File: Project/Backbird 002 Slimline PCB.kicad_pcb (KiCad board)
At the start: 2 copper layers, 14 x 116 mm, 8 parts

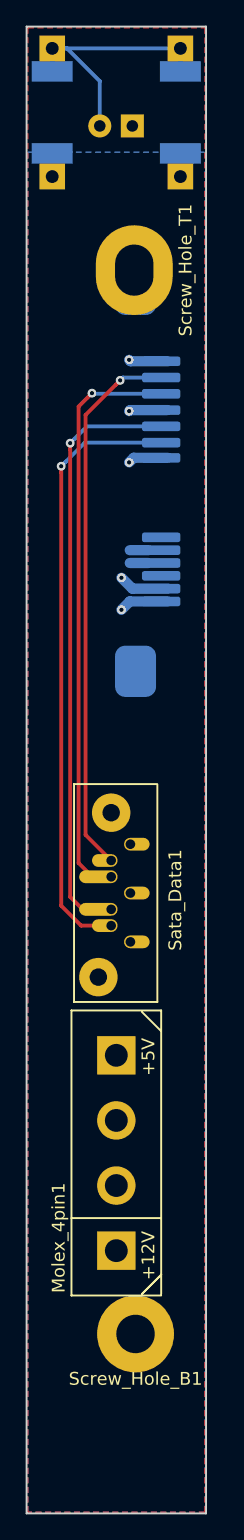
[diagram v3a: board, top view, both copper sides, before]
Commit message: Updated silkscreen to include description
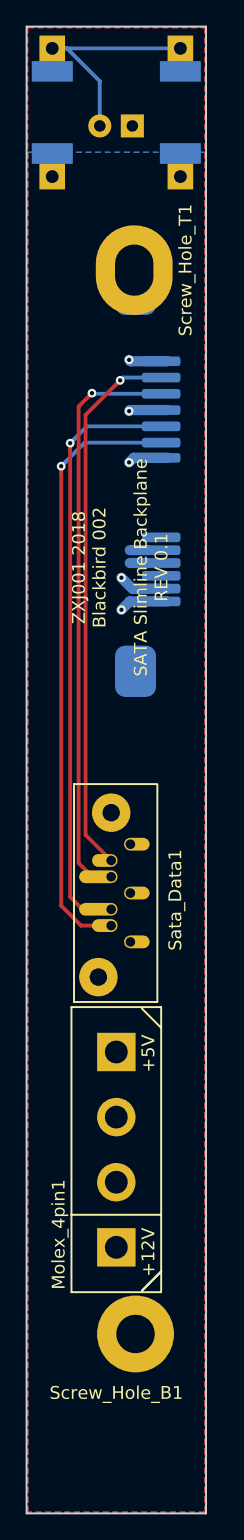
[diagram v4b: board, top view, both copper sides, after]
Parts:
- moved Molex_4pin1 0.26 mm to (107.3, 118.1)
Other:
- board text added: "ZXJ001 2018 Blackbird 002 SATA Slimline Backplane REV 0.1"
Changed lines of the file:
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@@
   (general
     (thickness 1.6)
-    (drawings 23)
+    (drawings 24)
     (tracks 60)
     (zones 0)
@@
   (page A4)
   (layers
-    (0 F.Cu signal hide)
+    (0 F.Cu signal)
     (31 B.Cu signal)
     (32 B.Adhes user)
     (33 F.Adhes user)
-    (34 B.Paste user)
-    (35 F.Paste user)
-    (36 B.SilkS user)
+    (34 B.Paste user hide)
+    (35 F.Paste user hide)
+    (36 B.SilkS user hide)
     (37 F.SilkS user)
     (38 B.Mask user)
@@
     (40 Dwgs.User user)
     (41 Cmts.User user)
-    (42 Eco1.User user)
-    (43 Eco2.User user)
+    (42 Eco1.User user hide)
+    (43 Eco2.User user hide)
     (44 Edge.Cuts user)
     (45 Margin user)
@@
   )
   (module ProjectFootprints:MOLEX_8981_0015244745 (layer F.Cu)
-    (at 107.3 118.36 90)
+    (at 107.3 118.1 90)
     (fp_text reference Molex_4pin1 (at -6.62 -4.5 90) (layer F.SilkS)
       (effects (font (size 1 1) (thickness 0.15)))
@@
   (module ProjectFootprints:Blackbird002_Slimline_PCB_Screw (layer F.Cu)
     (at 108.8 132.48)
-    (fp_text reference Screw_Hole_B1 (at 0 3.5) (layer F.SilkS)
+    (fp_text reference Screw_Hole_B1 (at -1.5 4.6) (layer F.SilkS)
       (effects (font (size 1 1) (thickness 0.15)))
     )
@@
     (pad 1 thru_hole oval (at 0 0 90) (size 7 6) (drill oval 4 3) (layers *.Cu *.Mask)
       (net 11 "Net-(Screw_Hole_T1-Pad1)"))
+  )
+  (gr_text "ZXJ001 2018\nBlackbird 002\n\nSATA Slimline Backplane\nREV 0.1" (at 107.6 72.68 90) (layer F.SilkS)
+    (effects (font (size 1 1) (thickness 0.2)))
   )
   (dimension 4 (width 0.3) (layer Eco1.User)
@@
   (segment (start 108.41 56.59) (end 108.3 56.48) (width 0.8) (layer B.Cu) (net 2))
   (segment (start 111.3 56.59) (end 108.41 56.59) (width 0.8) (layer B.Cu) (net 2))
+  (segment (start 112.3 40.3808) (end 112.3 42.18166) (width 0.3) (layer B.Cu) (net 2))
+  (segment (start 107.7 75.98) (end 108.35 75.33) (width 0.8) (layer B.Cu) (net 2))
+  (via (at 107.7 75.98) (size 0.6858) (drill 0.3302) (layers F.Cu B.Cu) (net 2))
+  (segment (start 108.35 75.33) (end 111.3 75.33) (width 0.8) (layer B.Cu) (net 2))
   (via (at 107.7 73.48) (size 0.6858) (drill 0.3302) (layers F.Cu B.Cu) (net 2))
+  (segment (start 108.55 74.33) (end 111.3 74.33) (width 0.8) (layer B.Cu) (net 2))
   (segment (start 107.7 73.48) (end 108.55 74.33) (width 0.8) (layer B.Cu) (net 2))
-  (segment (start 108.55 74.33) (end 111.3 74.33) (width 0.8) (layer B.Cu) (net 2))
-  (via (at 107.7 75.98) (size 0.6858) (drill 0.3302) (layers F.Cu B.Cu) (net 2))
-  (segment (start 107.7 75.98) (end 108.35 75.33) (width 0.8) (layer B.Cu) (net 2))
-  (segment (start 108.35 75.33) (end 111.3 75.33) (width 0.8) (layer B.Cu) (net 2))
-  (segment (start 112.3 40.3808) (end 112.3 42.18166) (width 0.3) (layer B.Cu) (net 2))
   (segment (start 109.8 71.33) (end 108.35 71.33) (width 0.8) (layer B.Cu) (net 3))
   (segment (start 109.8 72.33) (end 108.35 72.33) (width 0.8) (layer B.Cu) (net 3))
+  (segment (start 106.9 100.62) (end 104.555067 100.62) (width 0.3) (layer F.Cu) (net 4))
+  (segment (start 103 65.264933) (end 103 64.78) (width 0.3) (layer F.Cu) (net 4))
+  (segment (start 103 99.064933) (end 103 65.264933) (width 0.3) (layer F.Cu) (net 4))
   (segment (start 104.555067 100.62) (end 103 99.064933) (width 0.3) (layer F.Cu) (net 4))
-  (segment (start 106.9 100.62) (end 104.555067 100.62) (width 0.3) (layer F.Cu) (net 4))
+  (via (at 103 64.78) (size 0.6858) (drill 0.3302) (layers F.Cu B.Cu) (net 4))
   (segment (start 103.342899 64.437101) (end 103 64.78) (width 0.3) (layer B.Cu) (net 4))
+  (segment (start 111.3 62.94) (end 104.84 62.94) (width 0.3) (layer B.Cu) (net 4))
   (segment (start 104.84 62.94) (end 103.342899 64.437101) (width 0.3) (layer B.Cu) (net 4))
-  (segment (start 103 99.064933) (end 103 65.264933) (width 0.3) (layer F.Cu) (net 4))
-  (segment (start 111.3 62.94) (end 104.84 62.94) (width 0.3) (layer B.Cu) (net 4))
-  (segment (start 103 65.264933) (end 103 64.78) (width 0.3) (layer F.Cu) (net 4))
-  (via (at 103 64.78) (size 0.6858) (drill 0.3302) (layers F.Cu B.Cu) (net 4))
   (segment (start 106.9 99.35) (end 106.238934 99.35) (width 0.1524) (layer F.Cu) (net 5))
+  (segment (start 111.3 61.67) (end 105.010002 61.67) (width 0.3) (layer B.Cu) (net 5))
+  (segment (start 105.010002 61.67) (end 104.042901 62.637101) (width 0.3) (layer B.Cu) (net 5))
   (via (at 103.700002 62.98) (size 0.6858) (drill 0.3302) (layers F.Cu B.Cu) (net 5))
-  (segment (start 105.010002 61.67) (end 104.042901 62.637101) (width 0.3) (layer B.Cu) (net 5))
-  (segment (start 111.3 61.67) (end 105.010002 61.67) (width 0.3) (layer B.Cu) (net 5))
+  (segment (start 104.67 99.35) (end 103.700002 98.380002) (width 0.3) (layer F.Cu) (net 5))
+  (segment (start 103.700002 63.464933) (end 103.700002 62.98) (width 0.3) (layer F.Cu) (net 5))
+  (segment (start 106.9 99.35) (end 104.67 99.35) (width 0.3) (layer F.Cu) (net 5))
   (segment (start 104.042901 62.637101) (end 103.700002 62.98) (width 0.3) (layer B.Cu) (net 5))
-  (segment (start 104.67 99.35) (end 103.700002 98.380002) (width 0.3) (layer F.Cu) (net 5))
-  (segment (start 106.9 99.35) (end 104.67 99.35) (width 0.3) (layer F.Cu) (net 5))
   (segment (start 103.700002 98.380002) (end 103.700002 63.464933) (width 0.3) (layer F.Cu) (net 5))
-  (segment (start 103.700002 63.464933) (end 103.700002 62.98) (width 0.3) (layer F.Cu) (net 5))
+  (segment (start 105.45 59.13) (end 105.4 59.08) (width 0.3) (layer B.Cu) (net 6))
+  (segment (start 104.357101 60.122899) (end 105.057101 59.422899) (width 0.3) (layer F.Cu) (net 6))
+  (segment (start 111.3 59.13) (end 105.45 59.13) (width 0.3) (layer B.Cu) (net 6))
+  (segment (start 106.9 96.81) (end 105.43 96.81) (width 0.3) (layer F.Cu) (net 6))
+  (segment (start 105.057101 59.422899) (end 105.4 59.08) (width 0.3) (layer F.Cu) (net 6))
+  (segment (start 104.357101 95.737101) (end 104.357101 60.122899) (width 0.3) (layer F.Cu) (net 6))
+  (segment (start 105.43 96.81) (end 104.357101 95.737101) (width 0.3) (layer F.Cu) (net 6))
   (via (at 105.4 59.08) (size 0.6858) (drill 0.3302) (layers F.Cu B.Cu) (net 6))
-  (segment (start 105.43 96.81) (end 104.357101 95.737101) (width 0.3) (layer F.Cu) (net 6))
-  (segment (start 111.3 59.13) (end 105.45 59.13) (width 0.3) (layer B.Cu) (net 6))
-  (segment (start 104.357101 95.737101) (end 104.357101 60.122899) (width 0.3) (layer F.Cu) (net 6))
-  (segment (start 104.357101 60.122899) (end 105.057101 59.422899) (width 0.3) (layer F.Cu) (net 6))
-  (segment (start 105.057101 59.422899) (end 105.4 59.08) (width 0.3) (layer F.Cu) (net 6))
-  (segment (start 105.45 59.13) (end 105.4 59.08) (width 0.3) (layer B.Cu) (net 6))
-  (segment (start 106.9 96.81) (end 105.43 96.81) (width 0.3) (layer F.Cu) (net 6))
-  (via (at 107.599992 58.08) (size 0.6858) (drill 0.3302) (layers F.Cu B.Cu) (net 7))
   (segment (start 107.819992 57.86) (end 107.599992 58.08) (width 0.3) (layer B.Cu) (net 7))
   (segment (start 111.3 57.86) (end 107.819992 57.86) (width 0.3) (layer B.Cu) (net 7))
   (segment (start 106.9 95.54) (end 104.9 93.54) (width 0.3) (layer F.Cu) (net 7))
-  (segment (start 107.257093 58.422899) (end 107.599992 58.08) (width 0.3) (layer F.Cu) (net 7))
+  (via (at 107.599992 58.08) (size 0.6858) (drill 0.3302) (layers F.Cu B.Cu) (net 7))
   (segment (start 104.9 93.54) (end 104.9 60.779992) (width 0.3) (layer F.Cu) (net 7))
   (segment (start 104.9 60.779992) (end 107.257093 58.422899) (width 0.3) (layer F.Cu) (net 7))
+  (segment (start 107.257093 58.422899) (end 107.599992 58.08) (width 0.3) (layer F.Cu) (net 7))
   (zone (net 3) (net_name +5V) (layer B.Cu) (hatch edge 0.508)
     (connect_pads (clearance 0.508))

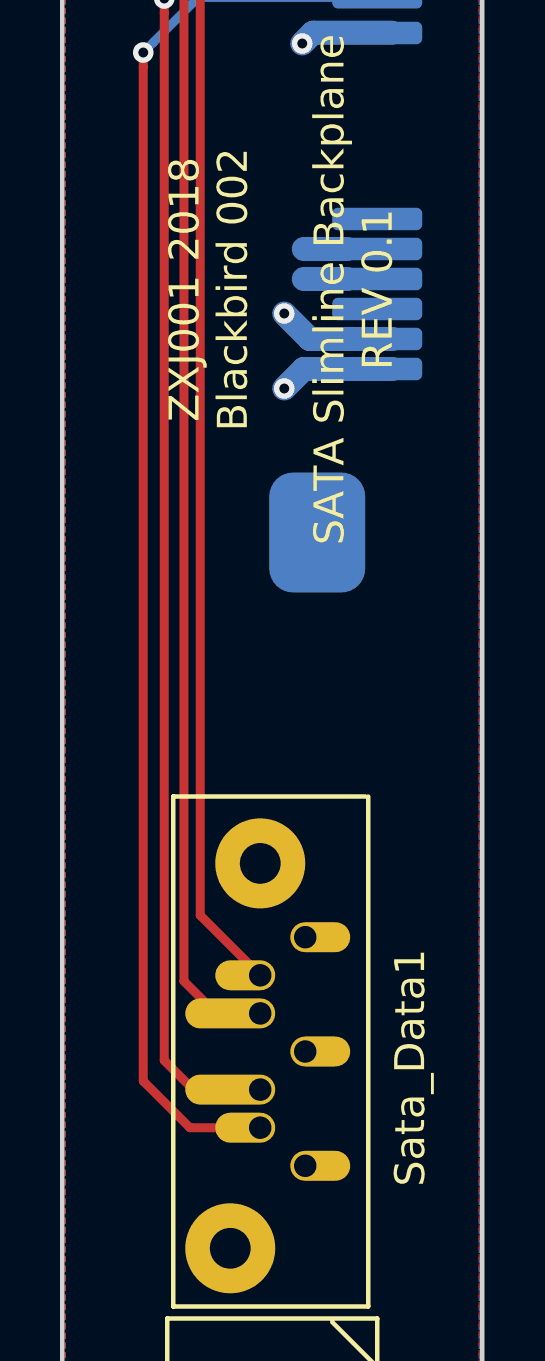
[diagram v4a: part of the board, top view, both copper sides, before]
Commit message: Fix SATA padding by having the drill in the center of the pad to meet OSHPark's expectations.
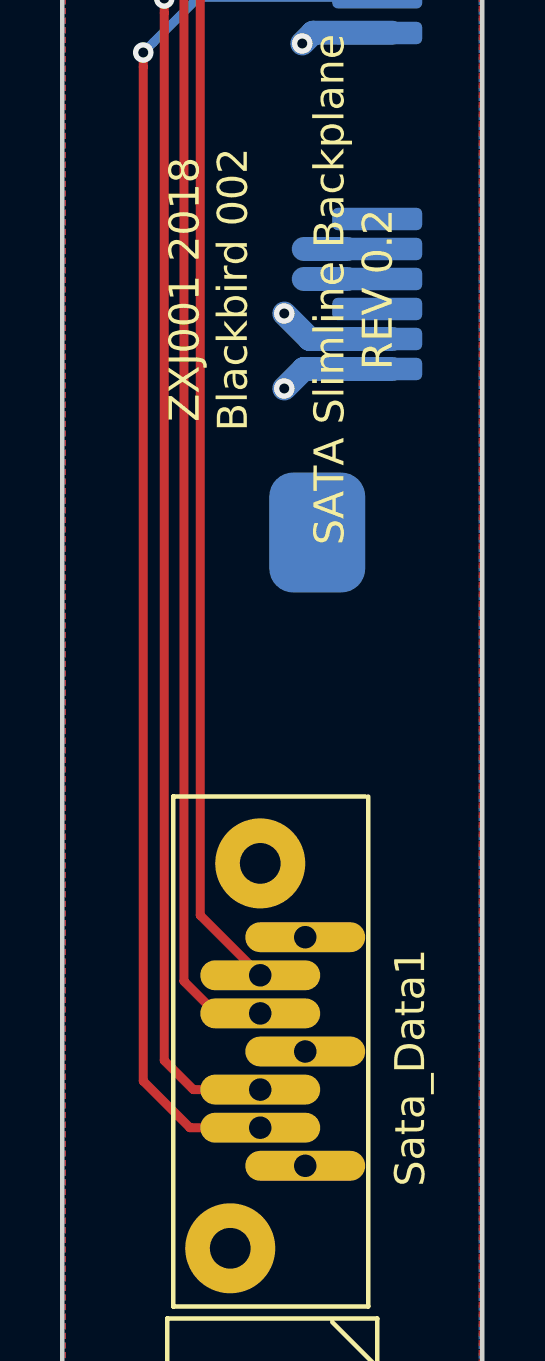
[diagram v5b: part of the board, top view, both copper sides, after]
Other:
- board text added: "ZXJ001 2018 Blackbird 002 SATA Slimline Backplane REV 0.2"
- board text removed: "ZXJ001 2018 Blackbird 002 SATA Slimline Backplane REV 0.1"
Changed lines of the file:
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@@
     (visible_elements FFFFFF7F)
     (pcbplotparams
-      (layerselection 0x010fc_ffffffff)
-      (usegerberextensions false)
+      (layerselection 0x010f0_ffffffff)
+      (usegerberextensions true)
       (usegerberattributes false)
       (usegerberadvancedattributes false)
@@
       (outputformat 1)
       (mirror false)
-      (drillshape 1)
+      (drillshape 0)
       (scaleselection 1)
-      (outputdirectory ""))
+      (outputdirectory Plots/))
   )
   (net 0 "")
@@
     (add_net "Net-(Screw_Hole_T1-Pad1)")
   )
+  (module ProjectFootprints:SATA_DATA_678007005_CustomPad (layer F.Cu)
+    (at 111.3 106.48 90)
+    (fp_text reference Sata_Data1 (at 7.86 0.6 90) (layer F.SilkS)
+      (effects (font (size 1 1) (thickness 0.15)))
+    )
+    (fp_text value Conn_01x07 (at 8.4 -9.504 90) (layer F.Fab)
+      (effects (font (size 1 1) (thickness 0.15)))
+    )
+    (fp_line (start 16.9 -7.3) (end 16.9 -0.9) (layer F.SilkS) (width 0.15))
+    (fp_line (start -0.1 -7.3) (end 16.9 -7.3) (layer F.SilkS) (width 0.15))
+    (fp_line (start -0.1 -0.8) (end -0.1 -7.3) (layer F.SilkS) (width 0.15))
+    (fp_line (start -0.1 -0.8) (end 16.9 -0.8) (layer F.SilkS) (width 0.15))
+    (pad 1 thru_hole oval (at 12.21 -2.9 270) (size 1 4) (drill 0.75) (layers *.Cu *.Mask)
+      (net 2 GND))
+    (pad 4 thru_hole oval (at 8.4 -2.9 270) (size 1 4) (drill 0.75) (layers *.Cu *.Mask)
+      (net 2 GND))
+    (pad 7 thru_hole oval (at 4.59 -2.9 270) (size 1 4) (drill 0.75) (layers *.Cu *.Mask)
+      (net 2 GND))
+    (pad 2 thru_hole oval (at 10.94 -4.4 90) (size 1 4) (drill 0.75) (layers *.Cu *.Mask)
+      (net 7 A+))
+    (pad 3 thru_hole oval (at 9.67 -4.4 90) (size 1 4) (drill 0.75) (layers *.Cu *.Mask)
+      (net 6 A-))
+    (pad 5 thru_hole oval (at 7.13 -4.4 90) (size 1 4) (drill 0.75) (layers *.Cu *.Mask)
+      (net 5 B-))
+    (pad 8 thru_hole circle (at 1.84 -5.4 90) (size 3 3) (drill 1.36) (layers *.Cu *.Mask))
+    (pad 8 thru_hole circle (at 14.67 -4.4 90) (size 3 3) (drill 1.36) (layers *.Cu *.Mask))
+    (pad 6 thru_hole oval (at 5.86 -4.4 90) (size 1 4) (drill 0.75) (layers *.Cu *.Mask)
+      (net 4 B+))
+  )
   (module ProjectFootprints:SATA_SLIMLINE_RECPT_1735539-2 (layer B.Cu)
     (at 108.8 65.88 90)
@@
     (pad 2 thru_hole rect (at 5.00126 0 90) (size 1.99898 1.99898) (drill 1.00076) (layers *.Cu *.Mask)
       (net 3 +5V))
-  )
-  (module ProjectFootprints:SATA_DATA_678007005_CustomPad (layer F.Cu)
-    (at 111.3 106.48 90)
-    (fp_text reference Sata_Data1 (at 7.86 0.6 90) (layer F.SilkS)
-      (effects (font (size 1 1) (thickness 0.15)))
-    )
-    (fp_text value Conn_01x07 (at 8.4 -9.504 90) (layer F.Fab)
-      (effects (font (size 1 1) (thickness 0.15)))
-    )
-    (fp_line (start 16.9 -7.3) (end 16.9 -0.9) (layer F.SilkS) (width 0.15))
-    (fp_line (start -0.1 -7.3) (end 16.9 -7.3) (layer F.SilkS) (width 0.15))
-    (fp_line (start -0.1 -0.8) (end -0.1 -7.3) (layer F.SilkS) (width 0.15))
-    (fp_line (start -0.1 -0.8) (end 16.9 -0.8) (layer F.SilkS) (width 0.15))
-    (pad 1 thru_hole oval (at 12.21 -2.9 270) (size 1 2) (drill 0.75 (offset 0 -0.5)) (layers *.Cu *.Mask)
-      (net 2 GND))
-    (pad 4 thru_hole oval (at 8.4 -2.9 270) (size 1 2) (drill 0.75 (offset 0 -0.5)) (layers *.Cu *.Mask)
-      (net 2 GND))
-    (pad 7 thru_hole oval (at 4.59 -2.9 270) (size 1 2) (drill 0.75 (offset 0 -0.5)) (layers *.Cu *.Mask)
-      (net 2 GND))
-    (pad 2 thru_hole oval (at 10.94 -4.4 90) (size 1 2) (drill 0.75 (offset 0 -0.5)) (layers *.Cu *.Mask)
-      (net 7 A+))
-    (pad 3 thru_hole oval (at 9.67 -4.4 90) (size 1 3) (drill 0.75 (offset 0 -1)) (layers *.Cu *.Mask)
-      (net 6 A-))
-    (pad 5 thru_hole oval (at 7.13 -4.4 90) (size 1 3) (drill 0.75 (offset 0 -1)) (layers *.Cu *.Mask)
-      (net 5 B-))
-    (pad 8 thru_hole circle (at 1.84 -5.4 90) (size 3 3) (drill 1.36) (layers *.Cu *.Mask))
-    (pad 8 thru_hole circle (at 14.67 -4.4 90) (size 3 3) (drill 1.36) (layers *.Cu *.Mask))
-    (pad 6 thru_hole oval (at 5.86 -4.4 90) (size 1 2) (drill 0.75 (offset 0 -0.5)) (layers *.Cu *.Mask)
-      (net 4 B+))
   )
   (module LEDs:LED_D1.8mm_W3.3mm_H2.4mm (layer B.Cu)
@@
       (net 11 "Net-(Screw_Hole_T1-Pad1)"))
   )
-  (gr_text "ZXJ001 2018\nBlackbird 002\n\nSATA Slimline Backplane\nREV 0.1" (at 107.6 72.68 90) (layer F.SilkS)
+  (gr_text "ZXJ001 2018\nBlackbird 002\n\nSATA Slimline Backplane\nREV 0.2" (at 107.6 72.68 90) (layer F.SilkS)
     (effects (font (size 1 1) (thickness 0.2)))
   )
@@
   (segment (start 109.8 71.33) (end 108.35 71.33) (width 0.8) (layer B.Cu) (net 3))
   (segment (start 109.8 72.33) (end 108.35 72.33) (width 0.8) (layer B.Cu) (net 3))
-  (segment (start 106.9 100.62) (end 104.555067 100.62) (width 0.3) (layer F.Cu) (net 4))
-  (segment (start 103 65.264933) (end 103 64.78) (width 0.3) (layer F.Cu) (net 4))
-  (segment (start 103 99.064933) (end 103 65.264933) (width 0.3) (layer F.Cu) (net 4))
-  (segment (start 104.555067 100.62) (end 103 99.064933) (width 0.3) (layer F.Cu) (net 4))
-  (via (at 103 64.78) (size 0.6858) (drill 0.3302) (layers F.Cu B.Cu) (net 4))
-  (segment (start 103.342899 64.437101) (end 103 64.78) (width 0.3) (layer B.Cu) (net 4))
-  (segment (start 111.3 62.94) (end 104.84 62.94) (width 0.3) (layer B.Cu) (net 4))
-  (segment (start 104.84 62.94) (end 103.342899 64.437101) (width 0.3) (layer B.Cu) (net 4))
+  (segment (start 104.84 62.94) (end 103.342899 64.437101) (width 0.3) (layer B.Cu) (net 4) (status 1000000))
+  (segment (start 103 65.264933) (end 103 64.78) (width 0.3) (layer F.Cu) (net 4) (status 1000000))
+  (segment (start 111.3 62.94) (end 104.84 62.94) (width 0.3) (layer B.Cu) (net 4) (status 1000000))
+  (segment (start 103.342899 64.437101) (end 103 64.78) (width 0.3) (layer B.Cu) (net 4) (status 1000000))
+  (segment (start 103 99.064933) (end 103 65.264933) (width 0.3) (layer F.Cu) (net 4) (status 1000000))
+  (segment (start 104.555067 100.62) (end 103 99.064933) (width 0.3) (layer F.Cu) (net 4) (status 1000000))
+  (segment (start 106.9 100.62) (end 104.555067 100.62) (width 0.3) (layer F.Cu) (net 4) (status 1000000))
+  (via (at 103 64.78) (size 0.6858) (drill 0.3302) (layers F.Cu B.Cu) (net 4) (status 1000000))
   (segment (start 106.9 99.35) (end 106.238934 99.35) (width 0.1524) (layer F.Cu) (net 5))
+  (segment (start 103.700002 63.464933) (end 103.700002 62.98) (width 0.3) (layer F.Cu) (net 5))
   (segment (start 111.3 61.67) (end 105.010002 61.67) (width 0.3) (layer B.Cu) (net 5))
   (segment (start 105.010002 61.67) (end 104.042901 62.637101) (width 0.3) (layer B.Cu) (net 5))
-  (via (at 103.700002 62.98) (size 0.6858) (drill 0.3302) (layers F.Cu B.Cu) (net 5))
-  (segment (start 104.67 99.35) (end 103.700002 98.380002) (width 0.3) (layer F.Cu) (net 5))
-  (segment (start 103.700002 63.464933) (end 103.700002 62.98) (width 0.3) (layer F.Cu) (net 5))
   (segment (start 106.9 99.35) (end 104.67 99.35) (width 0.3) (layer F.Cu) (net 5))
   (segment (start 104.042901 62.637101) (end 103.700002 62.98) (width 0.3) (layer B.Cu) (net 5))
+  (segment (start 104.67 99.35) (end 103.700002 98.380002) (width 0.3) (layer F.Cu) (net 5))
   (segment (start 103.700002 98.380002) (end 103.700002 63.464933) (width 0.3) (layer F.Cu) (net 5))
+  (via (at 103.700002 62.98) (size 0.6858) (drill 0.3302) (layers F.Cu B.Cu) (net 5))
+  (segment (start 111.3 59.13) (end 105.45 59.13) (width 0.3) (layer B.Cu) (net 6))
+  (segment (start 104.357101 60.122899) (end 105.057101 59.422899) (width 0.3) (layer F.Cu) (net 6))
   (segment (start 105.45 59.13) (end 105.4 59.08) (width 0.3) (layer B.Cu) (net 6))
-  (segment (start 104.357101 60.122899) (end 105.057101 59.422899) (width 0.3) (layer F.Cu) (net 6))
-  (segment (start 111.3 59.13) (end 105.45 59.13) (width 0.3) (layer B.Cu) (net 6))
+  (segment (start 105.057101 59.422899) (end 105.4 59.08) (width 0.3) (layer F.Cu) (net 6))
+  (segment (start 105.43 96.81) (end 104.357101 95.737101) (width 0.3) (layer F.Cu) (net 6))
+  (segment (start 104.357101 95.737101) (end 104.357101 60.122899) (width 0.3) (layer F.Cu) (net 6))
   (segment (start 106.9 96.81) (end 105.43 96.81) (width 0.3) (layer F.Cu) (net 6))
-  (segment (start 105.057101 59.422899) (end 105.4 59.08) (width 0.3) (layer F.Cu) (net 6))
-  (segment (start 104.357101 95.737101) (end 104.357101 60.122899) (width 0.3) (layer F.Cu) (net 6))
-  (segment (start 105.43 96.81) (end 104.357101 95.737101) (width 0.3) (layer F.Cu) (net 6))
   (via (at 105.4 59.08) (size 0.6858) (drill 0.3302) (layers F.Cu B.Cu) (net 6))
-  (segment (start 107.819992 57.86) (end 107.599992 58.08) (width 0.3) (layer B.Cu) (net 7))
+  (segment (start 106.9 95.54) (end 104.9 93.54) (width 0.3) (layer F.Cu) (net 7))
   (segment (start 111.3 57.86) (end 107.819992 57.86) (width 0.3) (layer B.Cu) (net 7))
-  (segment (start 106.9 95.54) (end 104.9 93.54) (width 0.3) (layer F.Cu) (net 7))
-  (via (at 107.599992 58.08) (size 0.6858) (drill 0.3302) (layers F.Cu B.Cu) (net 7))
-  (segment (start 104.9 93.54) (end 104.9 60.779992) (width 0.3) (layer F.Cu) (net 7))
   (segment (start 104.9 60.779992) (end 107.257093 58.422899) (width 0.3) (layer F.Cu) (net 7))
   (segment (start 107.257093 58.422899) (end 107.599992 58.08) (width 0.3) (layer F.Cu) (net 7))
+  (segment (start 104.9 93.54) (end 104.9 60.779992) (width 0.3) (layer F.Cu) (net 7))
+  (segment (start 107.819992 57.86) (end 107.599992 58.08) (width 0.3) (layer B.Cu) (net 7))
+  (via (at 107.599992 58.08) (size 0.6858) (drill 0.3302) (layers F.Cu B.Cu) (net 7))
   (zone (net 3) (net_name +5V) (layer B.Cu) (hatch edge 0.508)
     (connect_pads (clearance 0.508))
